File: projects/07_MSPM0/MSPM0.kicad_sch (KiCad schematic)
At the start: 50 parts, among them J1 USB_C_Receptacle_USB2.0_16P, J2 Conn_ARM_SWD_TagConnect_TC2030, U1 MSPM0G3507SPTR, U3 SPX3819M5-L-3-3, U4 CH340E, U5 LSM6DSR, U7 MMC5983MA, Y1 8MHz

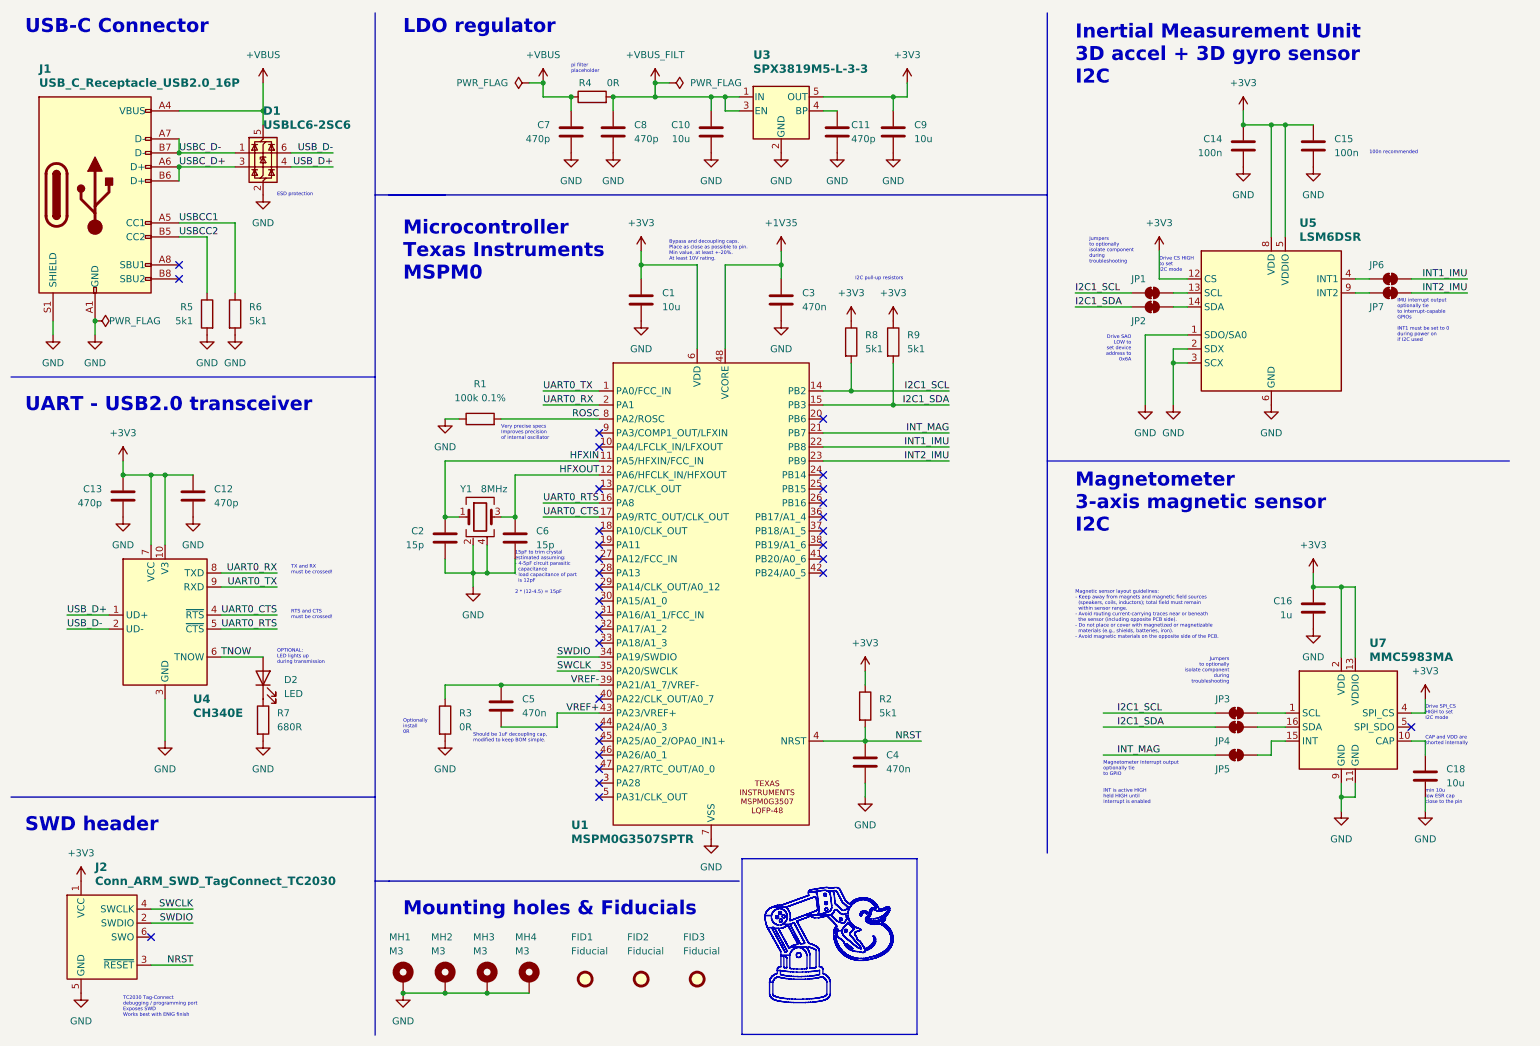
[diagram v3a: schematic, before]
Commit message: MSPM0 - Reassign pins. Add QWIIC connector for I2C. Finish placement.
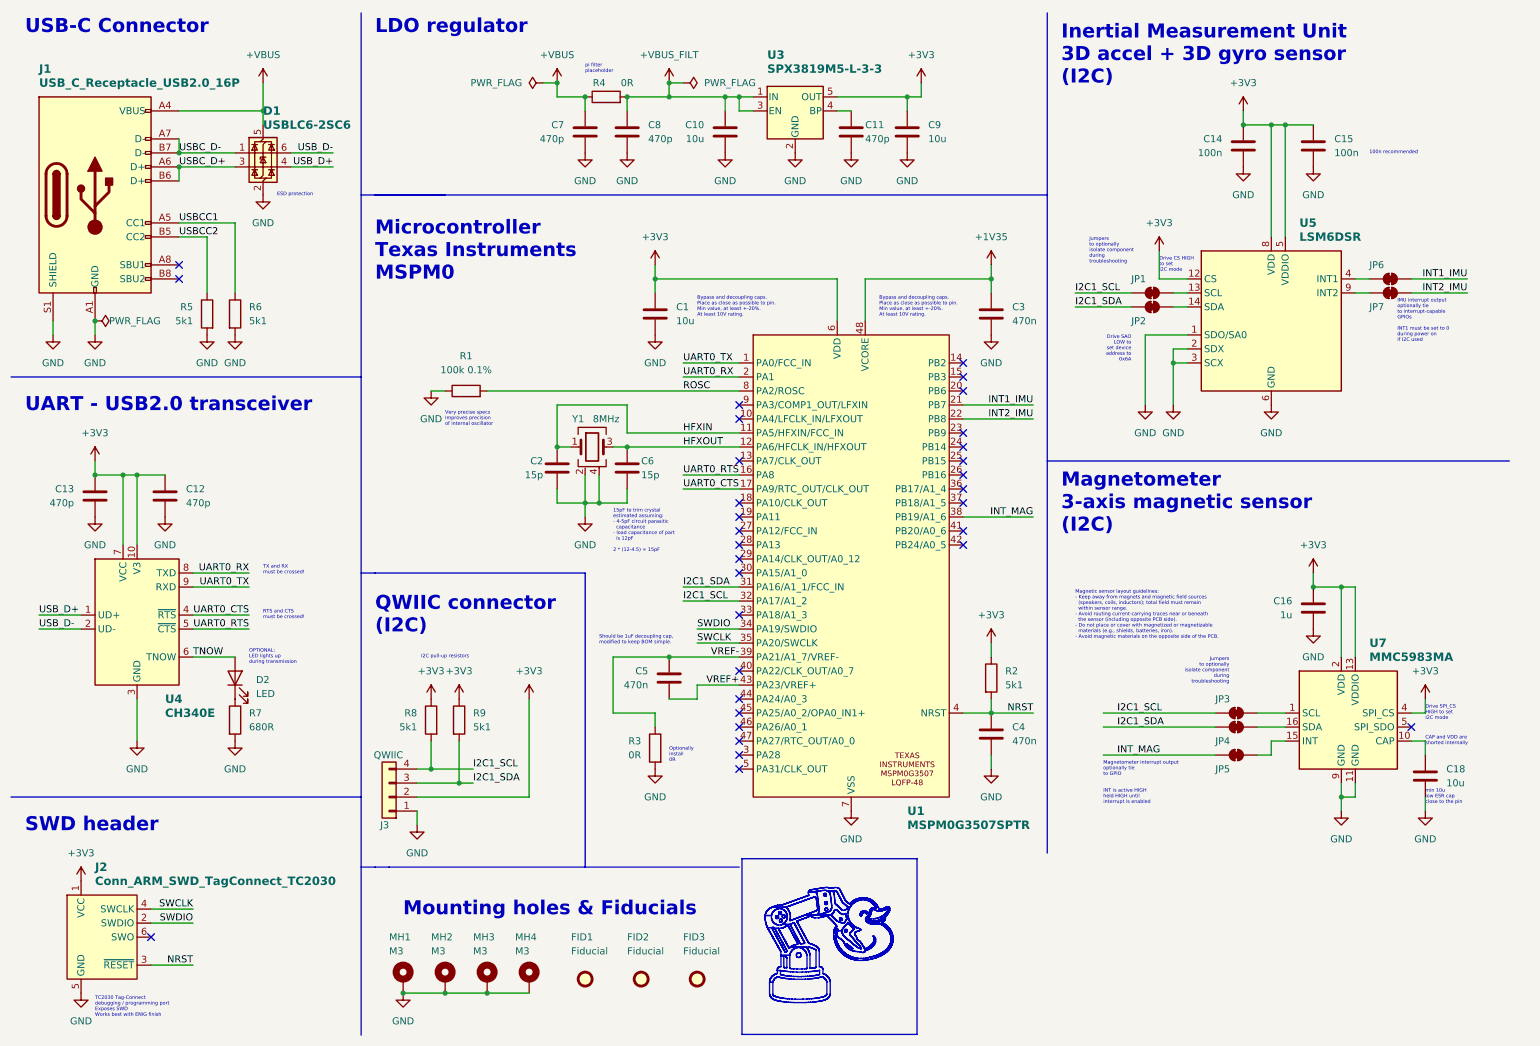
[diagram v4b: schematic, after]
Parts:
- added J3: QWIIC, Connector_JST:JST_SH_SM04B-SRSS-TB_1x04-1MP_P1.00mm_Horizontal, symbol MH_QWIIC:QWIIC
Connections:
- net +3V3: now also J3.2 (Pin_2)
- net GND: now also J3.1 (Pin_1)
- net I2C1_SCL: now also U1.32 (PA17/A1_2), J3.4 (Pin_4); no longer U1.14 (PB2)
- net I2C1_SDA: now also U1.31 (PA16/A1_1/FCC_IN), J3.3 (Pin_3); no longer U1.15 (PB3)
- net INT1_IMU: now also U1.21 (PB7); no longer U1.22 (PB8)
- net INT2_IMU: now also U1.22 (PB8); no longer U1.23 (PB9)
- net INT_MAG: now also U1.38 (PB19/A1_6); no longer U1.21 (PB7)
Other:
- note added: "Inertial Measurement Unit 3D accel + 3D gyro sensor (I2C)"
- note added: "Magnetometer 3-axis magnetic sensor (I2C)"
- note added: "QWIIC connector (I2C)"
- note removed: "Inertial Measurement Unit 3D accel + 3D gyro sensor I2C"
- note removed: "Magnetometer 3-axis magnetic sensor I2C"
- moved on the sheet: C1, C10, C11, C12, C13, C2, C3, C4, C5, C6, C7, C8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
